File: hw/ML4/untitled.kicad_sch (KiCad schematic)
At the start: 10 parts, among them J3 Conn_01x20, Q1 DMG2305UX-13, SW0 TS04-66-55-BK-160-SMT, U7 LM4040DBZ-3

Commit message: Updates for ML4
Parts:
- R17, R20: value 220 -> 100
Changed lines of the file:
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@@
 			)
 		)
-		(property "Value" "220"
+		(property "Value" "100"
 			(at 229.87 111.76 0)
 			(effects
@@
 			)
 		)
-		(property "Value" "220"
+		(property "Value" "100"
 			(at 215.9 111.76 0)
 			(effects

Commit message: Working on JCSC BOM
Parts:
- R17, R20: LCSC (none) -> C17408

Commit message: Working on adding LCSC part numbers
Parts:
- D3: LCSC (none) -> C2293
- D4: LCSC (none) -> C2297
- Q1: LCSC (none) -> C144153
- S1: LCSC (none) -> C7203003
- SW0: LCSC (none) -> C4364775
- U7: value LM4040DBZ-3 -> LM4040D30IDBZR; LCSC (none) -> C2157213
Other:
- note added: "This is a 3VDC voltage reference for the ADC"
- note removed: "This is a voltage reference for the ADC"
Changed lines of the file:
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@@
 	(title_block
 		(title "MicroLink - Microcontroller")
-		(date "2024-04-24")
+		(date "2025-09-30")
 		(rev "4")
 		(company "Bruce MacKinnon KC1FSZ")
 		(comment 1 "Copyright (C) 2024 - Not For Commercial Use")
 	)
-	(text "This is a voltage reference for the ADC"
+	(text "This is a 3VDC voltage reference for the ADC"
 		(exclude_from_sim no)
 		(at 177.546 72.136 0)
@@
 			)
 		)
-		(property "LCSC" ""
+		(property "LCSC" "C4364775"
 			(at 184.15 140.97 0)
 			(effects
@@
 			)
 		)
-		(property "LCSC" ""
+		(property "LCSC" "C7203003"
 			(at 115.57 100.33 0)
 			(effects
@@
 			)
 		)
-		(property "LCSC" ""
+		(property "LCSC" "C2293"
 			(at 213.36 116.84 0)
 			(effects
@@
 					(size 1.27 1.27)
 				)
+				(hide yes)
 			)
 		)
@@
 			)
 		)
-		(property "LCSC" ""
+		(property "LCSC" "C144153"
 			(at 162.56 45.72 0)
 			(effects
@@
 					(size 1.27 1.27)
 				)
+				(hide yes)
 			)
 		)
@@
 					(size 1.27 1.27)
 				)
+				(hide yes)
 			)
 		)
@@
 					(size 1.27 1.27)
 				)
+				(hide yes)
 			)
 		)
@@
 			)
 		)
-		(property "Value" "LM4040DBZ-3"
+		(property "Value" "LM4040D30IDBZR"
 			(at 173.99 78.74 90)
 			(effects
@@
 			)
 		)
-		(property "LCSC" ""
+		(property "LCSC" "C2157213"
 			(at 171.45 77.47 0)
 			(effects
@@
 					(size 1.27 1.27)
 				)
+				(hide yes)
 			)
 		)
@@
 			)
 		)
-		(property "LCSC" ""
+		(property "LCSC" "C2297"
 			(at 227.33 116.84 0)
 			(effects
@@
 					(size 1.27 1.27)
 				)
-			)
-		)
+				(hide yes)
+			)
+		)

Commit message: Working on adding LCSC part numbers
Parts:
- Q1: footprint Package_TO_SOT_SMD:SOT-23-3 -> digikey-footprints:SOT-23-3
- SW0: footprint bruce-footprints:SW_TS04-66-55-BK-160-SMT -> TS04-66-55-BK-160-SMT:SW_TS04-66-55-BK-160-SMT
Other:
- note added: "Pico Pi W Module"
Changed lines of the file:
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@@
+		)
+	)
+	(text "Pico Pi W Module"
+		(exclude_from_sim no)
+		(at 116.078 49.784 0)
+		(effects
+			(font
+				(size 1.27 1.27)
+			)
 		)
 	)
@@
 			)
 		)
-		(property "Footprint" "bruce-footprints:SW_TS04-66-55-BK-160-SMT"
+		(property "Footprint" "TS04-66-55-BK-160-SMT:SW_TS04-66-55-BK-160-SMT"
 			(at 184.15 140.97 0)
 			(effects
@@
 					(size 1.27 1.27)
 				)
+				(hide yes)
 			)
 		)
@@
 					(size 1.27 1.27)
 				)
+				(hide yes)
+			)
+		)
+		(property "DK" ""
+			(at 115.57 100.33 0)
+			(effects
+				(font
+					(size 1.27 1.27)
+				)
+				(hide yes)
 			)
 		)
@@
 			)
 		)
+		(property "Sim.Pins" "1=K 2=A"
+			(at 213.36 116.84 0)
+			(effects
+				(font
+					(size 1.27 1.27)
+				)
+				(hide yes)
+			)
+		)
 		(pin "2"
 		)
@@
 			)
 		)
-		(property "Footprint" "Package_TO_SOT_SMD:SOT-23-3"
+		(property "Footprint" "digikey-footprints:SOT-23-3"
 			(at 167.64 50.8 0)
 			(effects
@@
 		(pin "2"
 		)
+		(pin "3"
+		)
 		(instances
 			(project "ML4"
@@
 			(at 227.33 116.84 0)
 			(effects
+				(font
+					(size 1.27 1.27)
+				)
+				(hide yes)
+			)
+		)
+		(property "Sim.Pins" "1=K 2=A"
+			(at 227.33 116.84 0)
+			(effects

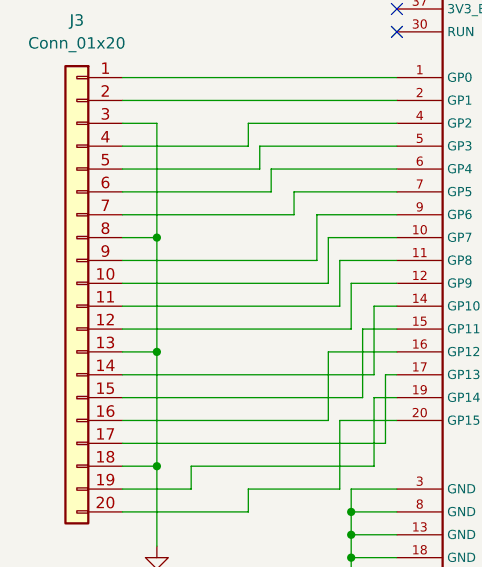
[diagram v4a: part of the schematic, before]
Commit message: Working on adding LCSC part numbers
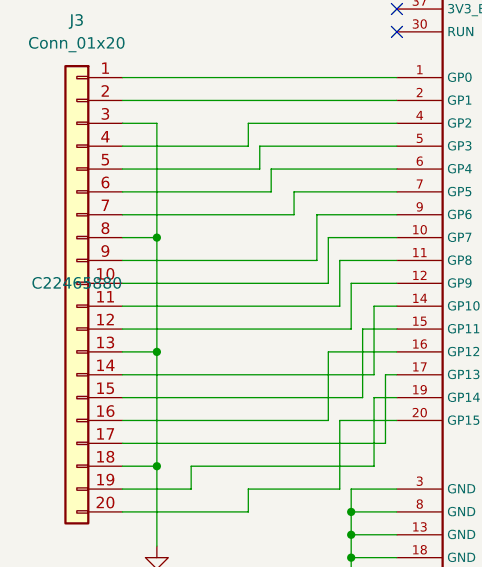
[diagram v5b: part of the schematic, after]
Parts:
- J3: BOM Comments (none) -> Standard 2.54mm pin header; LCSC (none) -> C22465880
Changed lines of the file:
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@@
 			)
 		)
-		(property "LCSC" ""
+		(property "LCSC" "C22465880"
 			(at 54.61 96.52 0)
 			(effects
@@
 			)
 		)
+		(property "BOM Comments" "Standard 2.54mm pin header"
+			(at 54.61 96.52 0)
+			(effects
+				(font
+					(size 1.27 1.27)
+				)
+				(hide yes)
+			)
+		)

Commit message: Working on ML4
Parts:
- D3: LCSC C2293 -> C84259
- Q1: footprint digikey-footprints:SOT-23-3 -> Package_TO_SOT_SMD:SOT-23_Handsoldering
- SW0: footprint TS04-66-55-BK-160-SMT:SW_TS04-66-55-BK-160-SMT -> bruce-footprints:SW_TS04-66-55-BK-160-SMT
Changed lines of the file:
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@@
 			)
 		)
-		(property "Footprint" "TS04-66-55-BK-160-SMT:SW_TS04-66-55-BK-160-SMT"
+		(property "Footprint" "bruce-footprints:SW_TS04-66-55-BK-160-SMT"
 			(at 184.15 140.97 0)
 			(effects
@@
 		)
 		(property "LCSC" "C4364775"
+			(at 184.15 140.97 0)
+			(effects
+				(font
+					(size 1.27 1.27)
+				)
+				(hide yes)
+			)
+		)
+		(property "DK" ""
+			(at 184.15 140.97 0)
+			(effects
+				(font
+					(size 1.27 1.27)
+				)
+				(hide yes)
+			)
+		)
+		(property "BOM Comments" ""
 			(at 184.15 140.97 0)
 			(effects
@@
 		)
 		(property "DK" ""
+			(at 115.57 100.33 0)
+			(effects
+				(font
+					(size 1.27 1.27)
+				)
+				(hide yes)
+			)
+		)
+		(property "BOM Comments" ""
 			(at 115.57 100.33 0)
 			(effects
@@
 			)
 		)
-		(property "LCSC" "C2293"
+		(property "LCSC" "C84259 "
 			(at 213.36 116.84 0)
 			(effects
@@
 			)
 		)
-		(property "Footprint" "digikey-footprints:SOT-23-3"
+		(property "Footprint" "Package_TO_SOT_SMD:SOT-23_Handsoldering"
 			(at 167.64 50.8 0)
 			(effects
